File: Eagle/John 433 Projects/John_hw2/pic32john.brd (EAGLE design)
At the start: 50 x 50 mm, 26 parts

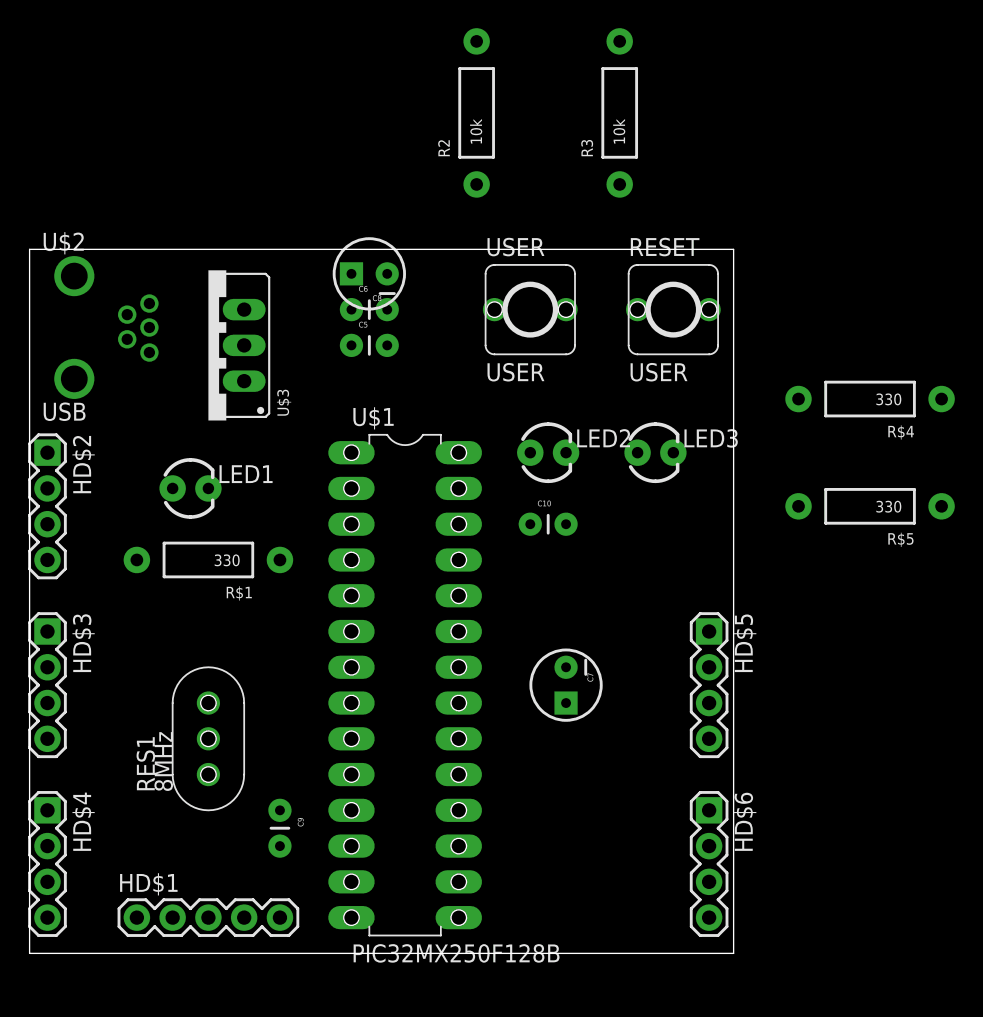
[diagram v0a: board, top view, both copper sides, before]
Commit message: layout mod unrouted
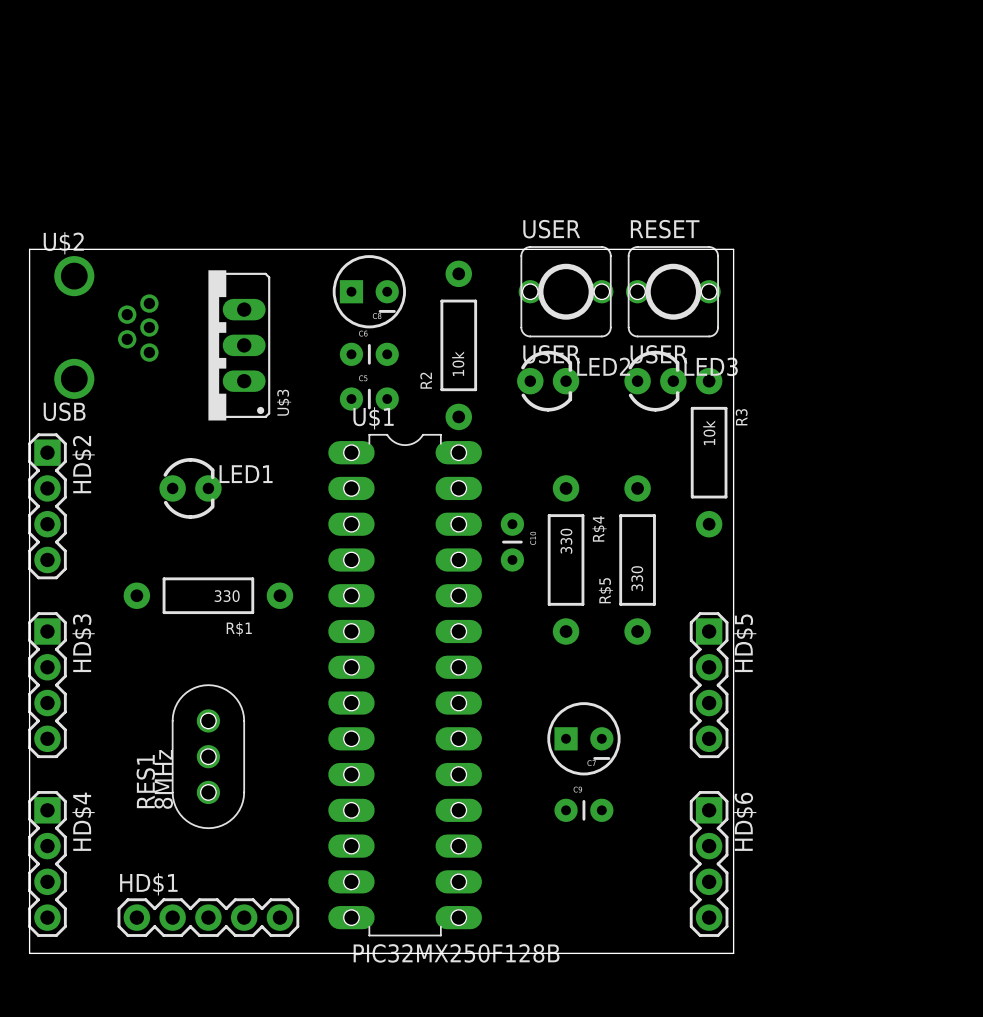
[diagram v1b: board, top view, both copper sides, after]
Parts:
- moved R3 25.0 mm to (48.3, 35.6), turned to 270 degrees
- moved R$4 24.4 mm to (38.1, 27.9), turned to 270 degrees
- moved C9 20.3 mm to (38.1, 10.2), turned to 0 degrees
- moved R$5 16.9 mm to (43.2, 27.9), turned to 90 degrees
- moved R2 16.6 mm to (30.5, 43.2)
- moved LED2 5.08 mm to (36.8, 40.6)
- moved LED3 5.08 mm to (44.5, 40.6)
- moved C7 4.02 mm to (39.4, 15.2), turned to 180 degrees
- moved C5 3.81 mm to (22.9, 39.4)
- moved C6 3.17 mm to (22.9, 42.5)
- moved USER 2.84 mm to (35.6, 47.0)
- moved R$1 2.54 mm to (12.7, 25.4)
- moved C10 1.27 mm to (34.3, 30.5), turned to 270 degrees
- moved RESET 1.27 mm to (43.2, 47.0)
- moved RES1 1.27 mm to (12.7, 11.4)
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
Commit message: done draft of board
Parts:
- moved R3 23.6 mm to (26.7, 45.1), turned to 180 degrees
- moved C9 21.1 mm to (17.1, 7.62), turned to 180 degrees
- moved LED1 18.2 mm to (27.9, 40.6), turned to 270 degrees
- moved R$4 9.67 mm to (47.0, 31.8)
- moved C8 8.98 mm to (17.8, 40.6), turned to 90 degrees
- moved LED3 8.89 mm to (35.6, 40.6)
- moved C5 8.13 mm to (17.8, 45.7), turned to 90 degrees
- moved LED2 6.35 mm to (43.2, 40.6)
- moved R$1 6.35 mm to (12.7, 31.8)
- moved R2 6.35 mm to (26.7, 48.3), turned to 180 degrees
- moved C10 5.08 mm to (34.3, 35.6)
- moved RESET 5.08 mm to (48.3, 47.0), turned to 180 degrees
- moved USER 5.08 mm to (40.6, 47.0), turned to 180 degrees
- moved R$5 4.02 mm to (41.9, 31.8)
- moved U$3 2.54 mm to (12.7, 43.2)
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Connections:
- net B14: now also HD$5.2
- net B15: now also R$5.P$2; no longer LED3.A
- net B4: no longer HD$5.2
- net B7: now also R$4.P$2; no longer LED2.A
- net GND: now also LED2.K, LED3.K; no longer R$4.P$1, R$5.P$1
- net N$4: now also LED2.A, R$4.P$1; no longer LED2.K, R$4.P$2
- net N$6: now also LED3.A, R$5.P$1; no longer LED3.K, R$5.P$2
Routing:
- net A0: track 0.00 -> 68.1 mm
- net A1: track 0.00 -> 63.0 mm
- net 3.3V: track 0.00 -> 51.1 mm
- net MCLR: track 0.00 -> 49.2 mm
- net B4: track 0.00 -> 30.0 mm, vias 0 -> 1
- net 5V: track 0.00 -> 27.1 mm
- net B13: track 0.00 -> 25.3 mm
- net B5: track 0.00 -> 23.7 mm
- net B3: track 0.00 -> 22.6 mm
- net B2: track 0.00 -> 22.6 mm
- net B1: track 0.00 -> 22.6 mm
- net A4: track 0.00 -> 22.6 mm
- net B0: track 0.00 -> 21.6 mm
- net B15: track 0.00 -> 20.9 mm
- net B14: track 0.00 -> 20.9 mm
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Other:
- board size 50 x 50 mm -> 50 x 52.5 mm

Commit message: first draft small changes
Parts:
- moved C10 2.54 mm to (36.8, 35.6)
- moved RES1 2.54 mm to (10.2, 11.4)
- turned LED3 to 180 degrees
- turned R$5 to 270 degrees
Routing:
- net 5V: track 27.1 -> 91.1 mm
- net 3.3V: track 51.1 -> 102.4 mm, vias 0 -> 1
- net USB.D-: track 0.00 -> 46.8 mm
- net USB.D+: track 0.00 -> 42.3 mm
- net MCLR: track 49.2 -> 85.6 mm
- net B13: track 25.3 -> 55.1 mm
- net B7: track 18.0 -> 39.4 mm
- net B15: track 20.9 -> 28.9 mm
- net N$4: track 0.00 -> 7.40 mm
- net N$6: track 0.00 -> 7.40 mm
- net N$2: track 10.7 -> 13.2 mm
- net N$1: track 10.7 -> 13.2 mm
- net A1: track 63.0 -> 61.0 mm
- added copper zone on layer 16, net GND
- added copper zone on layer 1, net TOPFILL
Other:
- board size 50 x 52.5 mm -> 50 x 50 mm

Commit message: draft 1 done and labelled
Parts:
- HD$1: value PIC_KIT -> PICkit3
- LED2: value (none) -> L1
- LED3: value (none) -> L2
- RST: value USER -> RST
- USER: value USER -> USR
- moved HD$1 1.27 mm to (8.89, 2.54)
- moved RES1 1.27 mm to (11.4, 11.4)
- moved U$1 1.27 mm to (24.1, 35.6)
- turned LED1 to 0 degrees
- turned LED3 to 0 degrees
- renumbered RESET to RST
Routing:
- net B13: track 55.1 -> 52.6 mm
- net N$3: track 15.5 -> 17.3 mm
- net N$6: track 7.40 -> 9.20 mm
- net USB.D+: track 42.3 -> 43.6 mm
- net A1: track 61.0 -> 62.2 mm
- net N$5: track 7.62 -> 6.35 mm
- net B8: track 18.4 -> 17.1 mm
- net B3: track 22.6 -> 23.9 mm
- net B2: track 22.6 -> 23.9 mm
- net B14: track 20.9 -> 19.7 mm
- net B1: track 22.6 -> 23.9 mm
- net B0: track 21.6 -> 22.9 mm
- net USB.D-: track 46.8 -> 48.1 mm
- net B9: track 19.0 -> 17.7 mm
- net B7: track 39.4 -> 38.1 mm
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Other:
- board text added: "A4 B5 GND 3.3V"
- board text added: "Apr 2015 v1"
- board text added: "B1 B2 B3 B4"
- board text added: "B15 B14 B13 B9"
- board text added: "B8 B7 GND +5V"
- board text added: "MCLR A0 A1 B0"
- board text added: "PIC32_433 JOHN T"

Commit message: board cam finished
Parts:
- moved U$3 1.27 mm to (14.0, 43.2)
- moved C5 1.27 mm to (19.1, 45.7)
- moved C8 1.27 mm to (19.1, 40.6)
- moved U$2 0.64 mm to (3.81, 44.5)
- moved R$1 0.63 mm to (12.1, 31.8)
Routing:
- net 5V: track 91.1 -> 93.7 mm
- net 3.3V: track 101.2 -> 99.9 mm
- net USB.D-: track 48.1 -> 48.9 mm
